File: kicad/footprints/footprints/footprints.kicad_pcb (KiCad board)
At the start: 2 copper layers, 9 parts

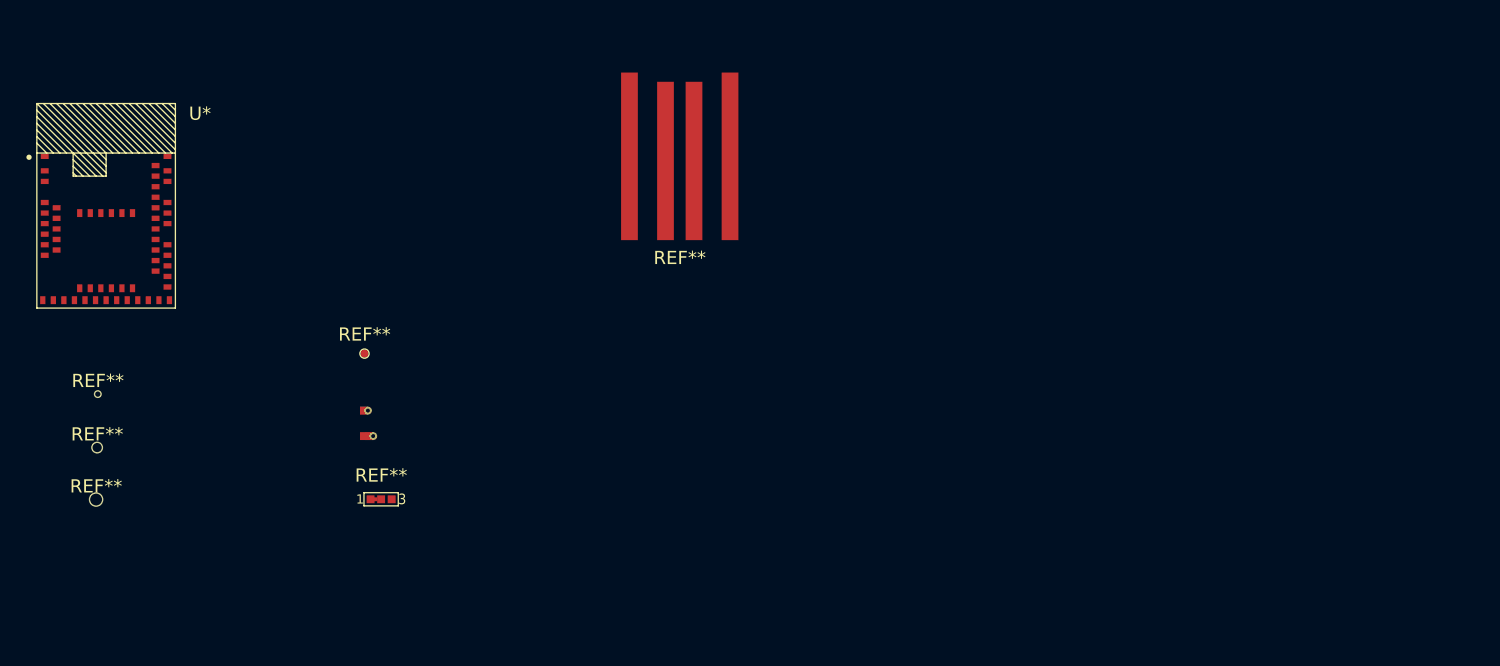
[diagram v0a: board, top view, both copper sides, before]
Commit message: added land pattern for carrier board
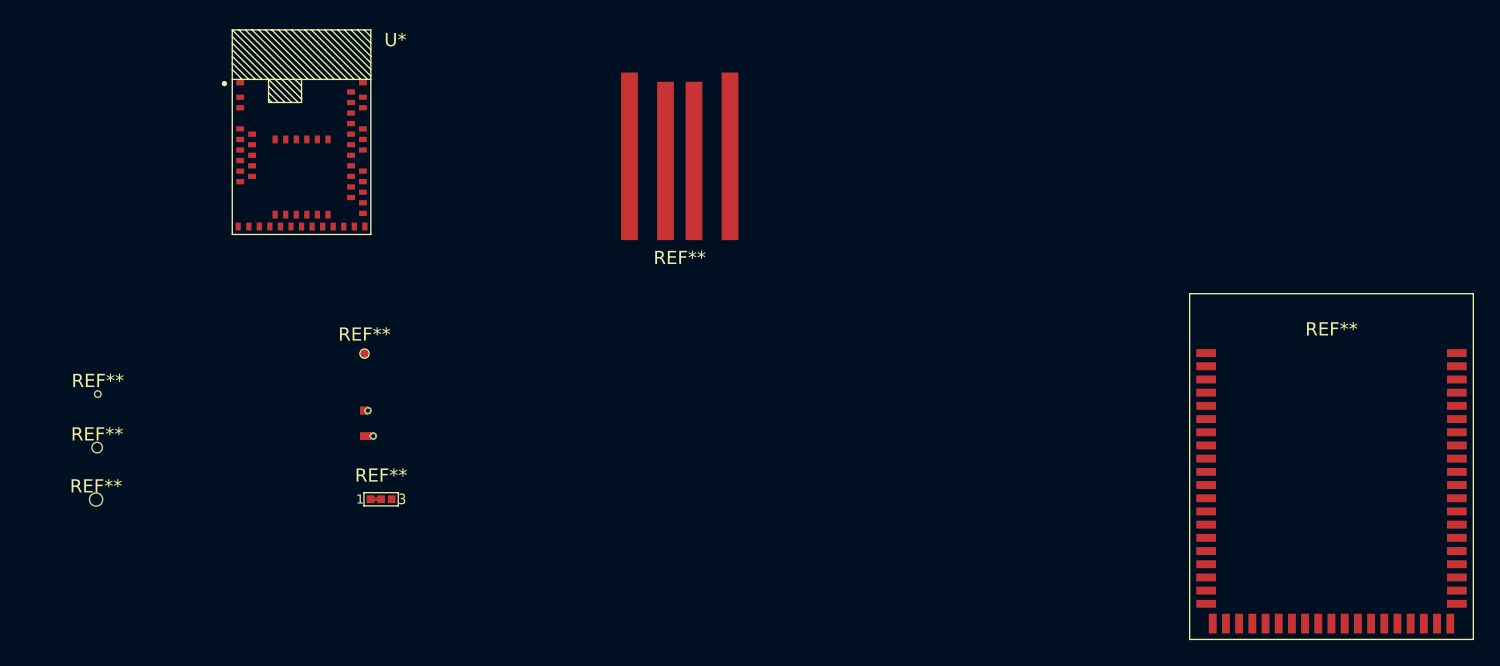
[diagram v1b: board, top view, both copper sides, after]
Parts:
- added REF**: MDBT50-land, MDBT50-land, F.Cu at (192.5, 105.5)
- moved U* 15.8 mm to (114.5, 88.5)
